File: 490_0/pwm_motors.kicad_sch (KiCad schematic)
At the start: 38 parts, among them J10 S2B-XH-A, J4 S2B-XH-A, J5 S2B-XH-A, J6 S2B-XH-A, J9 S2B-XH-A, Q1 NMOS, Q2 NMOS, Q3 NMOS, Q4 NMOS, Q5 NMOS, U6 PCA9685

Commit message: Changed 8conn and BOM update
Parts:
- C19, C21, C23, C25, C27, C30: footprint (none) -> Capacitor_SMD:C_0805_2012Metric
- C20, C22, C24, C26, C28, C31: footprint (none) -> Capacitor_SMD:C_1206_3216Metric
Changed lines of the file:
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@@
 			)
 		)
-		(property "Footprint" ""
+		(property "Footprint" "Capacitor_SMD:C_1206_3216Metric"
 			(at 191.4652 30.48 0)
 			(effects
@@
 			)
 		)
-		(property "Footprint" ""
+		(property "Footprint" "Capacitor_SMD:C_0805_2012Metric"
 			(at 181.9148 30.48 0)
 			(effects
@@
 			)
 		)
-		(property "Footprint" ""
+		(property "Footprint" "Capacitor_SMD:C_0805_2012Metric"
 			(at 42.2148 88.9 0)
 			(effects
@@
 			)
 		)
-		(property "Footprint" ""
+		(property "Footprint" "Capacitor_SMD:C_0805_2012Metric"
 			(at 115.8748 86.36 0)
 			(effects
@@
 			)
 		)
-		(property "Footprint" ""
+		(property "Footprint" "Capacitor_SMD:C_1206_3216Metric"
 			(at 69.5452 142.24 0)
 			(effects
@@
 			)
 		)
-		(property "Footprint" ""
+		(property "Footprint" "Capacitor_SMD:C_0805_2012Metric"
 			(at 59.9948 142.24 0)
 			(effects
@@
 			)
 		)
-		(property "Footprint" ""
+		(property "Footprint" "Capacitor_SMD:C_1206_3216Metric"
 			(at 51.7652 33.02 0)
 			(effects
@@
 			)
 		)
-		(property "Footprint" ""
+		(property "Footprint" "Capacitor_SMD:C_1206_3216Metric"
 			(at 122.8852 86.36 0)
 			(effects
@@
 			)
 		)
-		(property "Footprint" ""
+		(property "Footprint" "Capacitor_SMD:C_1206_3216Metric"
 			(at 119.0752 33.02 0)
 			(effects
@@
 			)
 		)
-		(property "Footprint" ""
+		(property "Footprint" "Capacitor_SMD:C_0805_2012Metric"
 			(at 109.5248 33.02 0)
 			(effects
@@
 			)
 		)
-		(property "Footprint" ""
+		(property "Footprint" "Capacitor_SMD:C_0805_2012Metric"
 			(at 44.7548 33.02 0)
 			(effects
@@
 			)
 		)
-		(property "Footprint" ""
+		(property "Footprint" "Capacitor_SMD:C_1206_3216Metric"
 			(at 49.2252 88.9 0)
 			(effects

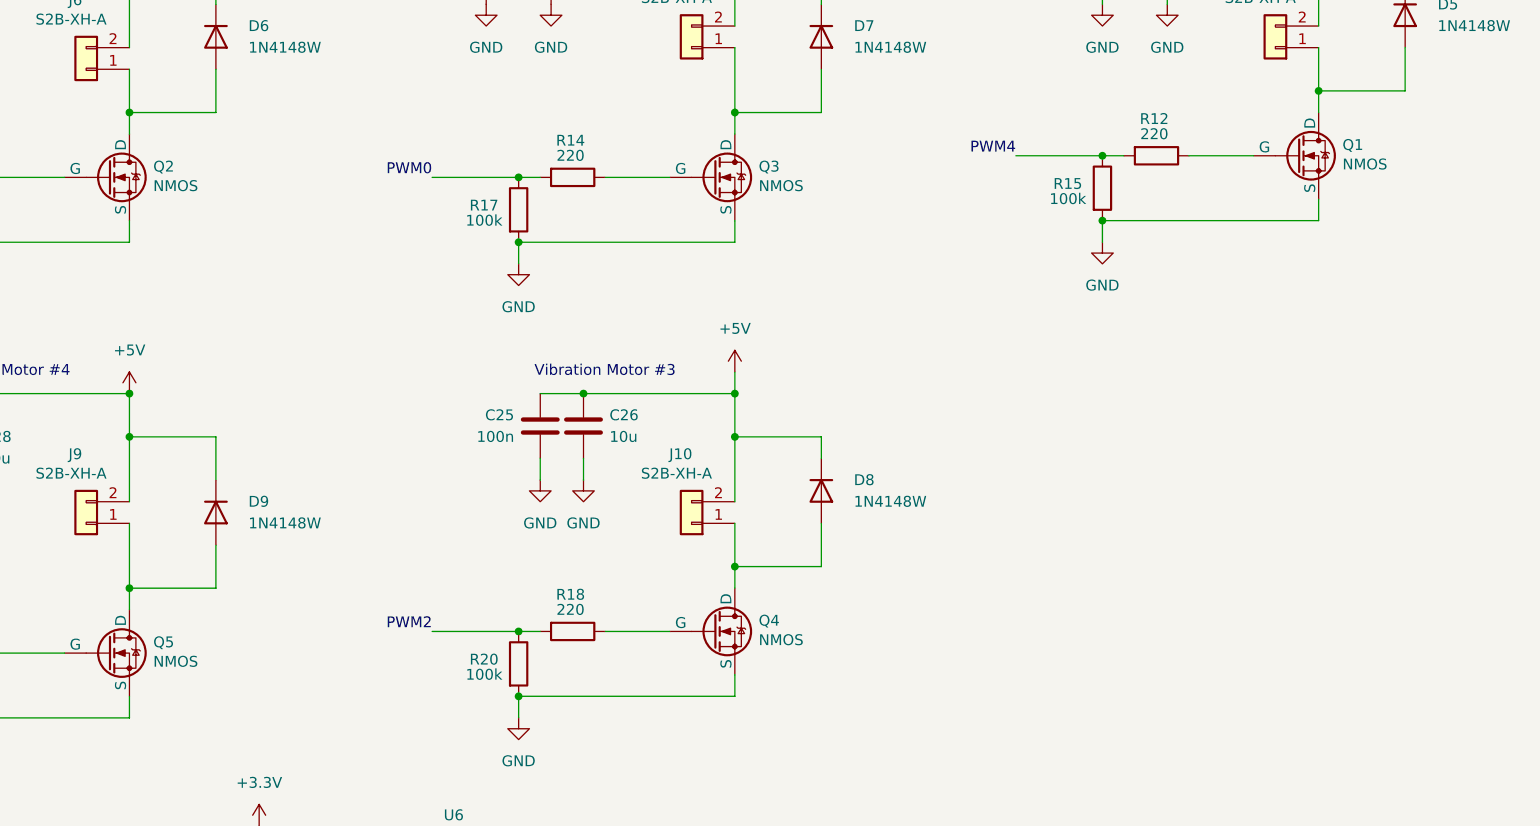
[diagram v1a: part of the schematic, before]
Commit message: LED names + 5V routing through ESD + renamed ESD chips to "U"
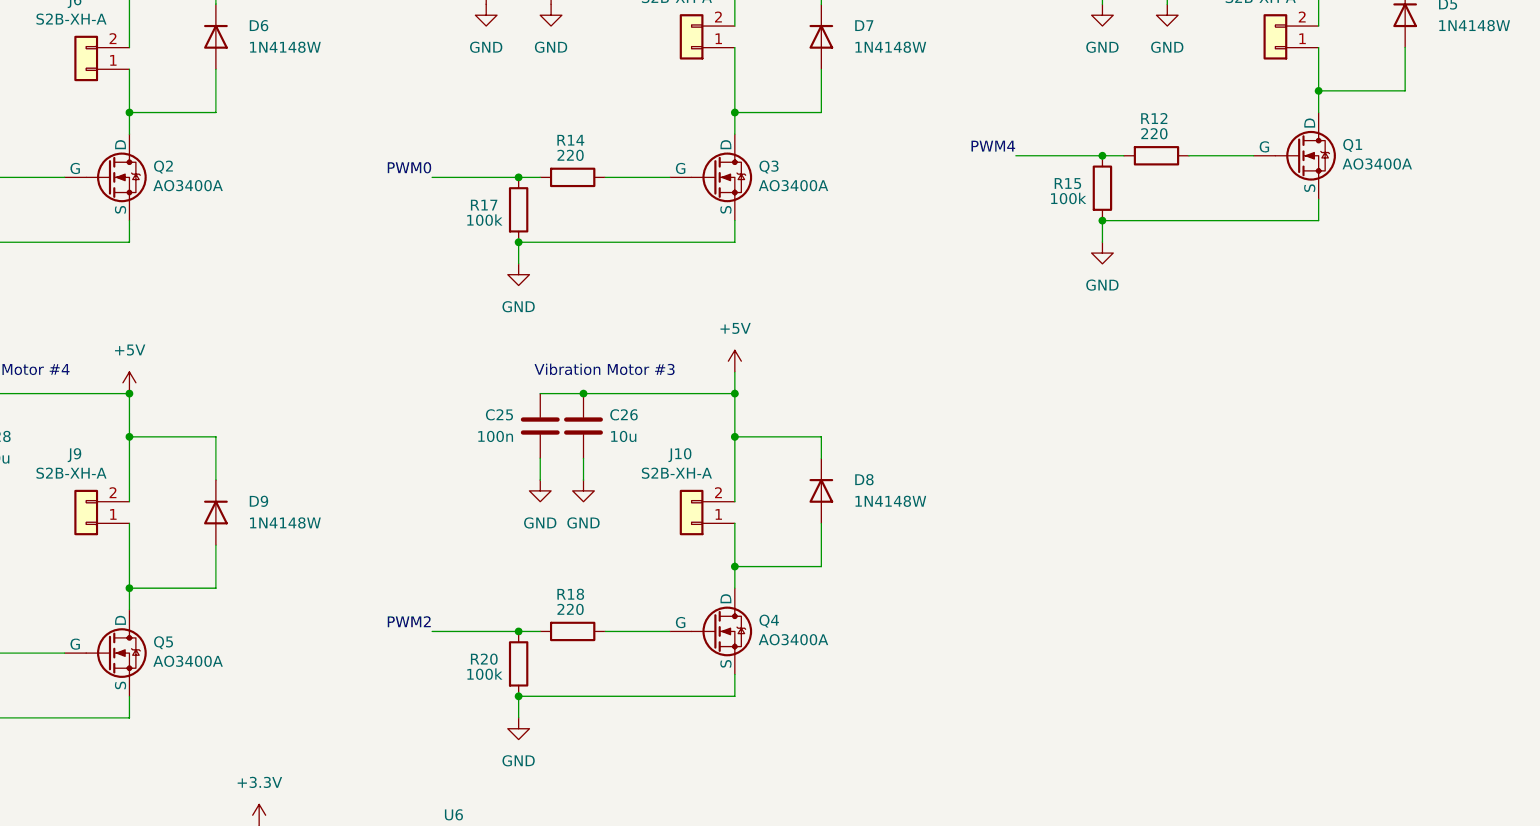
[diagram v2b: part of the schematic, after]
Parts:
- Q1, Q2, Q3, Q4, Q5: value NMOS -> AO3400A
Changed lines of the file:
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@@
 			)
 		)
-		(property "Value" "NMOS"
+		(property "Value" "AO3400A"
 			(at 142.494 107.696 0)
 			(effects
@@
 			)
 		)
-		(property "Value" "NMOS"
+		(property "Value" "AO3400A"
 			(at 211.074 51.816 0)
 			(effects
@@
 			)
 		)
-		(property "Value" "NMOS"
+		(property "Value" "AO3400A"
 			(at 71.374 54.356 0)
 			(effects
@@
 			)
 		)
-		(property "Value" "NMOS"
+		(property "Value" "AO3400A"
 			(at 71.374 110.236 0)
 			(effects
@@
 			)
 		)
-		(property "Value" "NMOS"
+		(property "Value" "AO3400A"
 			(at 142.494 54.356 0)
 			(effects

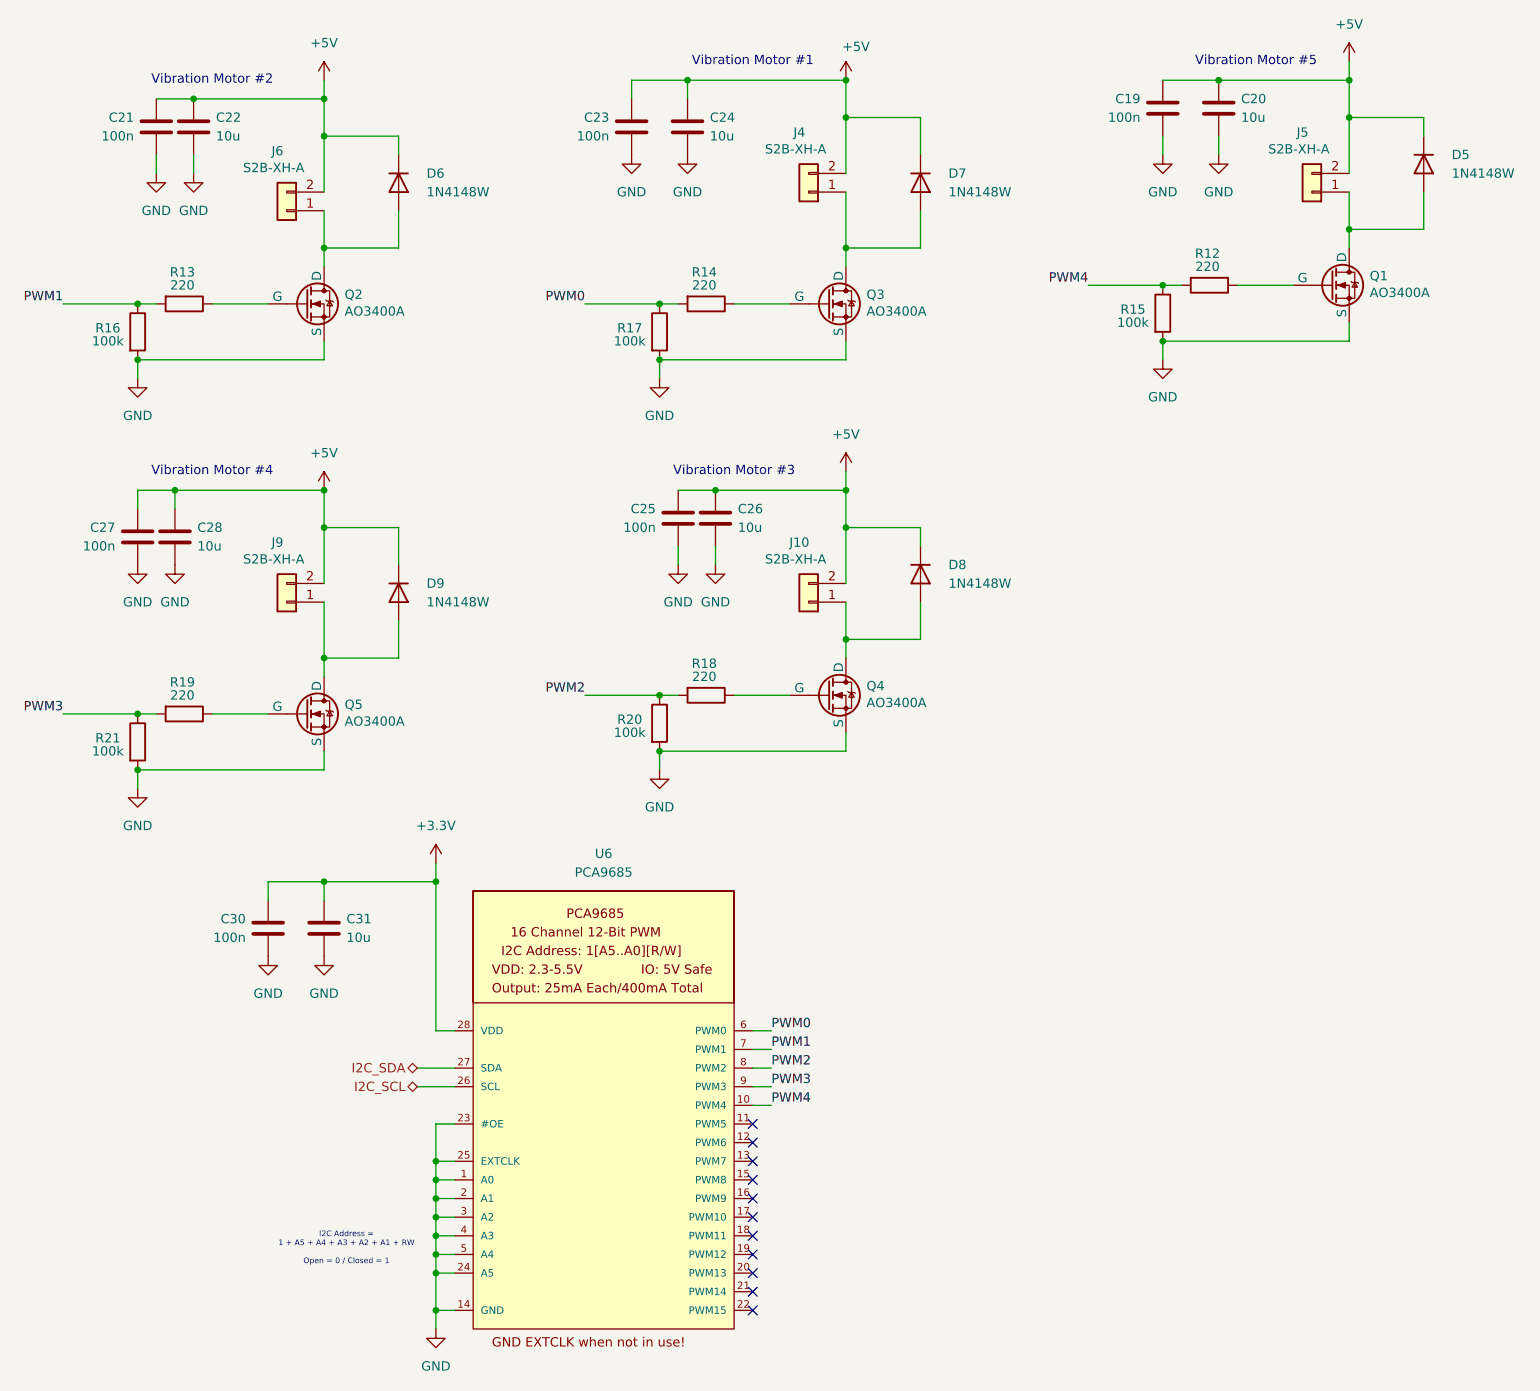
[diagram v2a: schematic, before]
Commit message: Fixed capacitor symbols
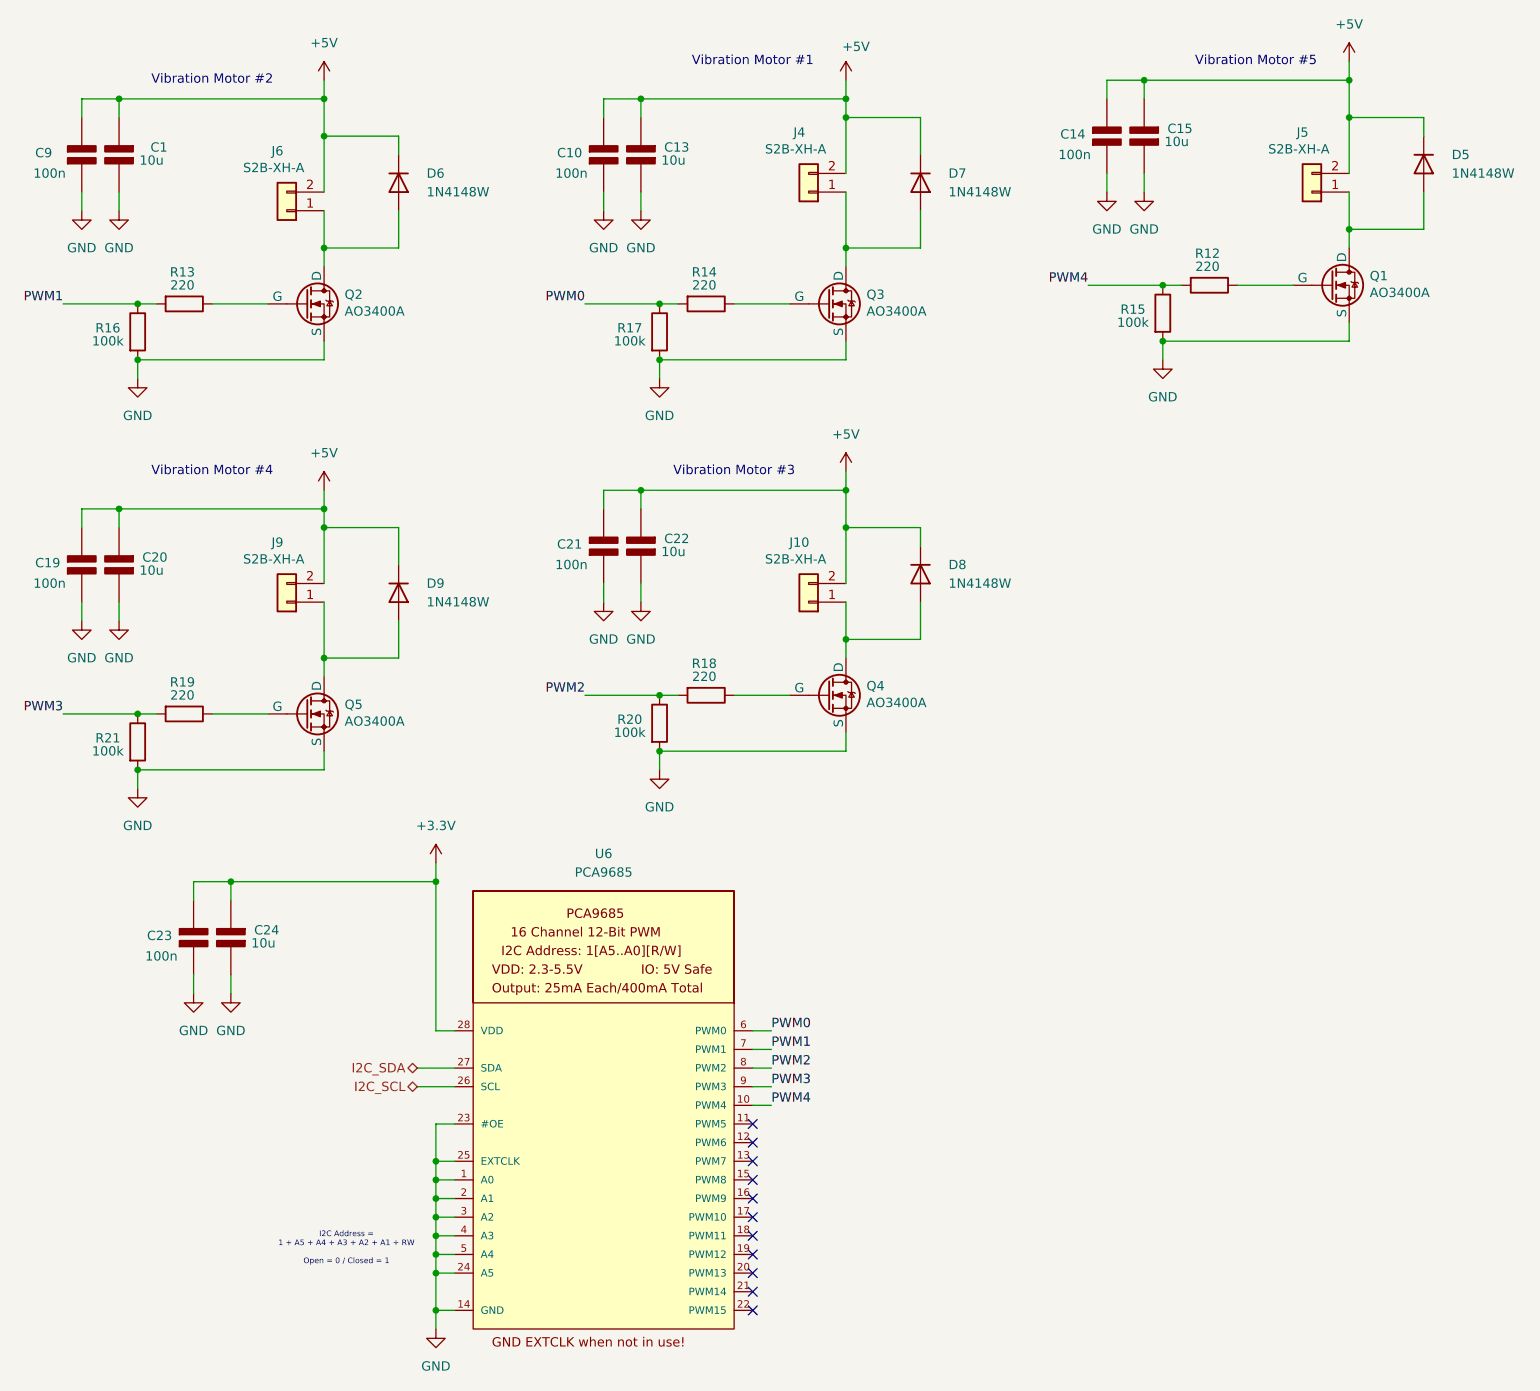
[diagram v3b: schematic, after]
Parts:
- removed C19, C21, C23, C25, C27, C30: 100n, Capacitor_SMD:C_0805_2012Metric, symbol Device:C
- removed C20, C22, C24, C26, C28, C31: 10u, Capacitor_SMD:C_1206_3216Metric, symbol Device:C
- added C1, C13, C15, C20, C22, C24: 10u, Capacitor_SMD:C_1206_3216Metric, symbol PCM_Elektuur:C
- added C10, C14, C19, C21, C23, C9: 100n, Capacitor_SMD:C_0805_2012Metric, symbol PCM_Elektuur:C
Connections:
- net +3.3V: now also C23.2 (-), C24.1 (+)
- net +5V: now also C1.1 (+), C10.2 (-), C13.1 (+), C14.2 (-), C15.1 (+), C19.2 (-), C20.1 (+), C21.2 (-), C22.1 (+), C9.2 (-)
- net GND: now also C1.2 (-), C10.1 (+), C13.2 (-), C14.1 (+), C15.2 (-), C19.1 (+), C20.2 (-), C21.1 (+), C22.2 (-), C23.1 (+), C24.2 (-), C9.1 (+)

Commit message: PCB Jumpstart
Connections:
- net +5V: now also D5.C (K), D6.C, D7.C (K), D8.C (K), D9.C (K); no longer D5.1 (K), D6.1 (K), D7.1 (K), D8.1 (K), D9.1 (K)
- net at J5.1 (Pin_1), Q1.1 (D): now also D5.A; no longer D5.2 (A)
- net at J9.1 (Pin_1), Q5.1 (D): now also D9.A; no longer D9.2 (A)
- net at J10.1 (Pin_1), Q4.1 (D): now also D8.A; no longer D8.2 (A)
- net at J6.1 (Pin_1), Q2.1 (D): now also D6.A; no longer D6.2 (A)
- net at J4.1 (Pin_1), Q3.1 (D): now also D7.A; no longer D7.2 (A)
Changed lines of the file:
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@@
 	)
 	(symbol
+		(lib_name "D_4")
 		(lib_id "Device:D")
 		(at 149.86 90.17 270)
@@
 			)
 		)
-		(pin "1"
+		(pin "C"
 		)
-		(pin "2"
+		(pin "A"
 		)
 		(instances
@@
 	)
 	(symbol
+		(lib_name "D_1")
 		(lib_id "Device:D")
 		(at 78.74 36.83 270)
@@
 			)
 		)
-		(pin "1"
+		(pin "C"
 		)
-		(pin "2"
+		(pin "A"
 		)
 		(instances
@@
 			)
 		)
-		(pin "1"
+		(pin "C"
 		)
-		(pin "2"
+		(pin "A"
 		)
 		(instances
@@
 	)
 	(symbol
+		(lib_name "D_3")
 		(lib_id "Device:D")
 		(at 149.86 36.83 270)
@@
 			)
 		)
-		(pin "1"
+		(pin "C"
 		)
-		(pin "2"
+		(pin "A"
 		)
 		(instances
@@
 	)
 	(symbol
+		(lib_name "D_2")
 		(lib_id "Device:D")
 		(at 218.44 34.29 270)
@@
 			)
 		)
-		(pin "1"
+		(pin "A"
 		)
-		(pin "2"
+		(pin "C"
 		)
 		(instances

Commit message: Post-Dmitry Changes
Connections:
- net GND: no longer C1.2 (-), C10.1 (+), C13.2 (-), C14.1 (+), C15.2 (-), C19.1 (+), C20.2 (-), C21.1 (+), C22.2 (-), C9.1 (+), Q1.3 (S), Q2.3 (S), Q3.3 (S), Q4.3 (S), Q5.3 (S), R15.2, R16.2, R17.2, R20.2, R21.2
- new net: Q1.3 (S), R15.2
- new net: Q3.3 (S), R17.2
- new net: Q2.3 (S), R16.2
- new net: Q5.3 (S), R21.2
- new net GNDD: Q4.3 (S), R20.2

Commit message: Added seperate ground for PWM motors
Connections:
- net GNDD: now also C1.2 (-), C10.1 (+), C13.2 (-), C14.1 (+), C15.2 (-), C19.1 (+), C20.2 (-), C21.1 (+), C22.2 (-), C9.1 (+), Q1.3 (S), Q2.3 (S), Q3.3 (S), Q5.3 (S), R15.2, R16.2, R17.2, R21.2
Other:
- moved on the sheet: C10, C14, C19, C21, C9

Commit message: Changed footprints for pad connectors (for soldered components)
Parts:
- J10, J4, J5, J6, J9: value S2B-XH-A -> PAD; footprint *CapStone*:JST_S2B-XH-A -> Connector_PinHeader_1.27mm:PinHeader_1x02_P1.27mm_Vertical
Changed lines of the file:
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@@
 			)
 		)
-		(property "Value" "S2B-XH-A"
+		(property "Value" "PAD"
 			(at 201.422 32.258 0)
 			(effects
@@
 			)
 		)
-		(property "Footprint" "*CapStone*:JST_S2B-XH-A"
+		(property "Footprint" "Connector_PinHeader_1.27mm:PinHeader_1x02_P1.27mm_Vertical"
 			(at 203.835 42.545 0)
 			(effects
@@
 			)
 		)
-		(property "Value" "S2B-XH-A"
+		(property "Value" "PAD"
 			(at 61.722 88.138 0)
 			(effects
@@
 			)
 		)
-		(property "Footprint" "*CapStone*:JST_S2B-XH-A"
+		(property "Footprint" "Connector_PinHeader_1.27mm:PinHeader_1x02_P1.27mm_Vertical"
 			(at 64.135 98.425 0)
 			(effects
@@
 			)
 		)
-		(property "Value" "S2B-XH-A"
+		(property "Value" "PAD"
 			(at 132.842 32.258 0)
 			(effects
@@
 			)
 		)
-		(property "Footprint" "*CapStone*:JST_S2B-XH-A"
+		(property "Footprint" "Connector_PinHeader_1.27mm:PinHeader_1x02_P1.27mm_Vertical"
 			(at 135.255 42.545 0)
 			(effects
@@
 			)
 		)
-		(property "Value" "S2B-XH-A"
+		(property "Value" "PAD"
 			(at 132.842 88.138 0)
 			(effects
@@
 			)
 		)
-		(property "Footprint" "*CapStone*:JST_S2B-XH-A"
+		(property "Footprint" "Connector_PinHeader_1.27mm:PinHeader_1x02_P1.27mm_Vertical"
 			(at 135.255 98.425 0)
 			(effects
@@
 			)
 		)
-		(property "Value" "S2B-XH-A"
+		(property "Value" "PAD"
 			(at 61.722 34.798 0)
 			(effects
@@
 			)
 		)
-		(property "Footprint" "*CapStone*:JST_S2B-XH-A"
+		(property "Footprint" "Connector_PinHeader_1.27mm:PinHeader_1x02_P1.27mm_Vertical"
 			(at 64.135 45.085 0)
 			(effects
